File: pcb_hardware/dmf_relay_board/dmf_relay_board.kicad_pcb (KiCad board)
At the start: 2 copper layers, 100 x 100 mm, 34 parts, among them J1 HVPS, J2 Relays to Electrodes 1, J3 Relays to Electrodes 2, J4 Electrodes from Relay 1, J5 Electrodes from Relay 2, U1 HV507

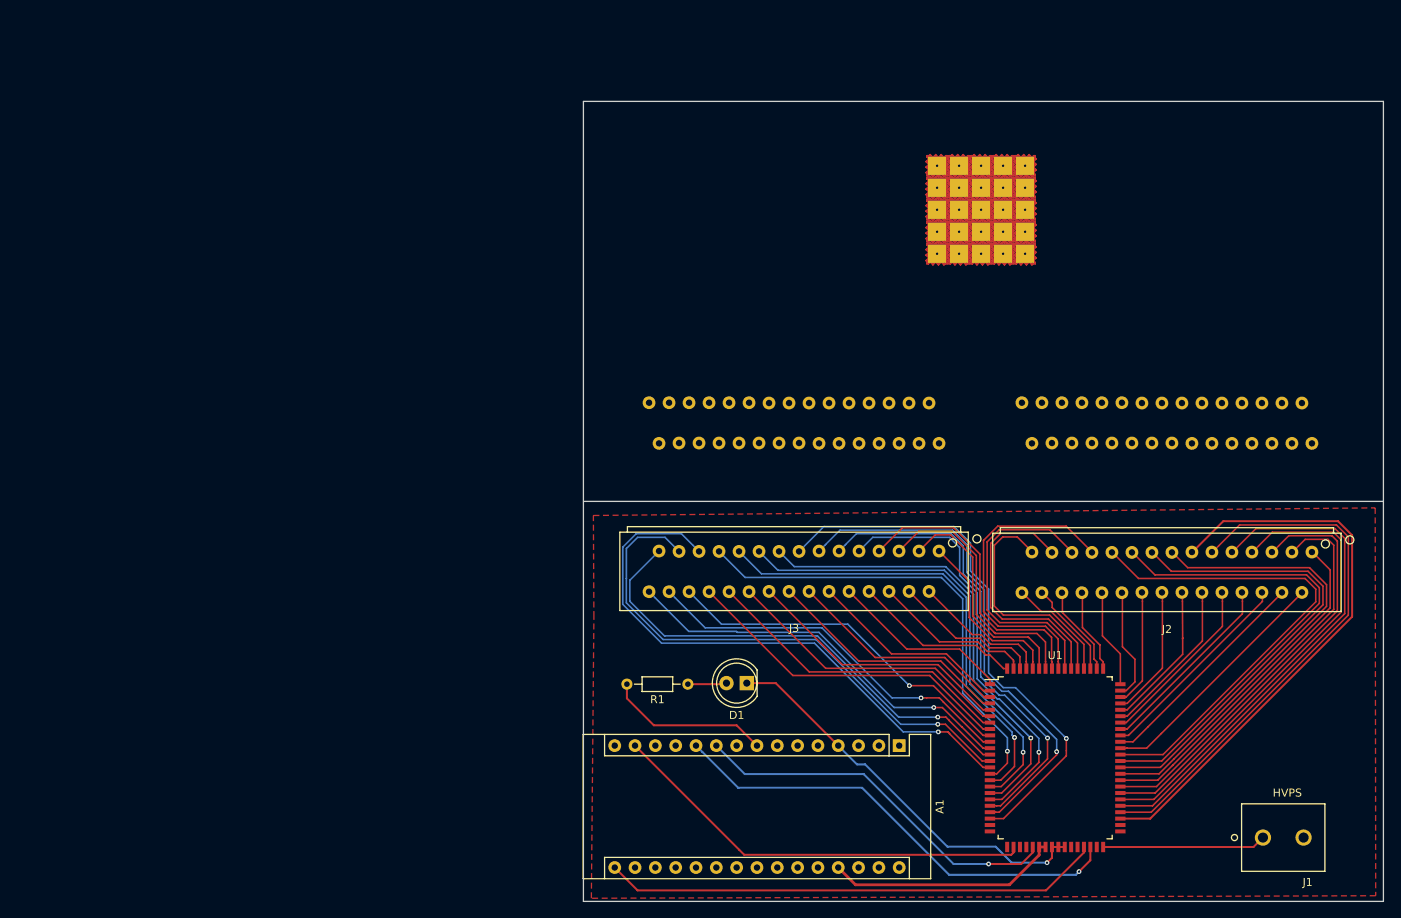
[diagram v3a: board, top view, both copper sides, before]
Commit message: electrode footprints created
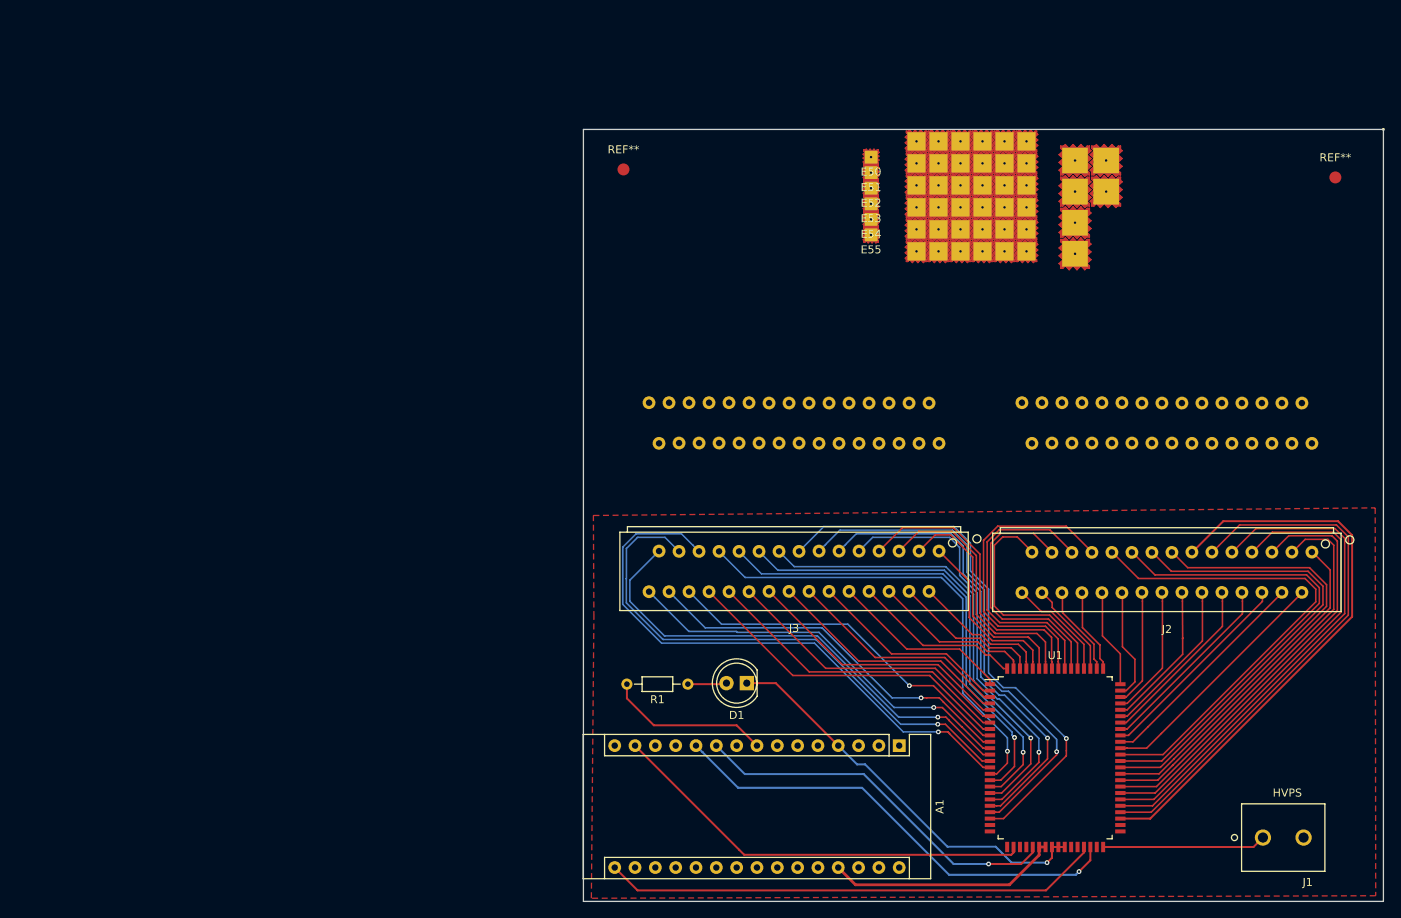
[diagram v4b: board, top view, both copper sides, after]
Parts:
- removed ELEC_1 (x25): FX, GaudiLabsFootPrints:FLUXPAD_2_75_4MIL_4_5
- added E1: ELEC_SML, dmf_relay_board:ELECTRODE_2_75_4MIL_4_5, F.Cu at (153.6, 55.5)
- added E10: ELEC_SML, dmf_relay_board:ELECTRODE_2_75_4MIL_4_5, F.Cu at (161.9, 58.3)
- added E11: ELEC_SML, dmf_relay_board:ELECTRODE_2_75_4MIL_4_5, F.Cu at (164.6, 58.3)
- added E12: ELEC_SML, dmf_relay_board:ELECTRODE_2_75_4MIL_4_5, F.Cu at (167.4, 58.3)
- added E13: ELEC_SML, dmf_relay_board:ELECTRODE_2_75_4MIL_4_5, F.Cu at (153.6, 61.0)
- added E14: ELEC_SML, dmf_relay_board:ELECTRODE_2_75_4MIL_4_5, F.Cu at (156.4, 61.0)
- added E15: ELEC_SML, dmf_relay_board:ELECTRODE_2_75_4MIL_4_5, F.Cu at (159.1, 61.0)
- added E16: ELEC_SML, dmf_relay_board:ELECTRODE_2_75_4MIL_4_5, F.Cu at (161.9, 61.0)
- added E17: ELEC_SML, dmf_relay_board:ELECTRODE_2_75_4MIL_4_5, F.Cu at (164.6, 61.0)
- added E18: ELEC_SML, dmf_relay_board:ELECTRODE_2_75_4MIL_4_5, F.Cu at (167.4, 61.0)
- added E19: ELEC_SML, dmf_relay_board:ELECTRODE_2_75_4MIL_4_5, F.Cu at (153.6, 63.8)
- added E2: ELEC_SML, dmf_relay_board:ELECTRODE_2_75_4MIL_4_5, F.Cu at (156.4, 55.5)
- added E20: ELEC_SML, dmf_relay_board:ELECTRODE_2_75_4MIL_4_5, F.Cu at (156.4, 63.8)
- added E21: ELEC_SML, dmf_relay_board:ELECTRODE_2_75_4MIL_4_5, F.Cu at (159.1, 63.8)
- added E22: ELEC_SML, dmf_relay_board:ELECTRODE_2_75_4MIL_4_5, F.Cu at (161.9, 63.8)
- added E23: ELEC_SML, dmf_relay_board:ELECTRODE_2_75_4MIL_4_5, F.Cu at (164.6, 63.8)
- added E24: ELEC_SML, dmf_relay_board:ELECTRODE_2_75_4MIL_4_5, F.Cu at (167.4, 63.8)
- added E25: ELEC_SML, dmf_relay_board:ELECTRODE_2_75_4MIL_4_5, F.Cu at (153.6, 66.5)
- added E26: ELEC_SML, dmf_relay_board:ELECTRODE_2_75_4MIL_4_5, F.Cu at (156.4, 66.5)
- added E27: ELEC_SML, dmf_relay_board:ELECTRODE_2_75_4MIL_4_5, F.Cu at (159.1, 66.5)
- added E28: ELEC_SML, dmf_relay_board:ELECTRODE_2_75_4MIL_4_5, F.Cu at (161.9, 66.5)
- added E29: ELEC_SML, dmf_relay_board:ELECTRODE_2_75_4MIL_4_5, F.Cu at (164.6, 66.5)
- added E3: ELEC_SML, dmf_relay_board:ELECTRODE_2_75_4MIL_4_5, F.Cu at (159.1, 55.5)
- added E30: ELEC_SML, dmf_relay_board:ELECTRODE_2_75_4MIL_4_5, F.Cu at (167.4, 66.5)
- added E31: ELEC_SML, dmf_relay_board:ELECTRODE_2_75_4MIL_4_5, F.Cu at (153.6, 69.3)
- added E32: ELEC_SML, dmf_relay_board:ELECTRODE_2_75_4MIL_4_5, F.Cu at (156.4, 69.3)
- added E33: ELEC_SML, dmf_relay_board:ELECTRODE_2_75_4MIL_4_5, F.Cu at (159.1, 69.3)
- added E34: ELEC_SML, dmf_relay_board:ELECTRODE_2_75_4MIL_4_5, F.Cu at (161.9, 69.3)
- added E35: ELEC_SML, dmf_relay_board:ELECTRODE_2_75_4MIL_4_5, F.Cu at (164.6, 69.3)
- added E36: ELEC_SML, dmf_relay_board:ELECTRODE_2_75_4MIL_4_5, F.Cu at (167.4, 69.3)
- added E4: ELEC_SML, dmf_relay_board:ELECTRODE_2_75_4MIL_4_5, F.Cu at (161.9, 55.5)
- added E5: ELEC_SML, dmf_relay_board:ELECTRODE_2_75_4MIL_4_5, F.Cu at (164.6, 55.5)
- added E50: ELEC_XS, dmf_relay_board:ELECTRODE_1_375_4MIL_4_5, F.Cu at (147.9, 57.5)
- added E51: ELEC_XS, dmf_relay_board:ELECTRODE_1_375_4MIL_4_5, F.Cu at (147.9, 59.4)
- added E52: ELEC_XS, dmf_relay_board:ELECTRODE_1_375_4MIL_4_5, F.Cu at (147.9, 61.4)
- added E53: ELEC_XS, dmf_relay_board:ELECTRODE_1_375_4MIL_4_5, F.Cu at (147.9, 63.3)
- added E54: ELEC_XS, dmf_relay_board:ELECTRODE_1_375_4MIL_4_5, F.Cu at (147.9, 65.3)
- added E55: ELEC_XS, dmf_relay_board:ELECTRODE_1_375_4MIL_4_5, F.Cu at (147.9, 67.2)
- added E6: ELEC_SML, dmf_relay_board:ELECTRODE_2_75_4MIL_4_5, F.Cu at (167.4, 55.5)
- added E60: ELEC_LG, dmf_relay_board:ELECTRODE_3_89_4MIL_4_5, F.Cu at (173.4, 57.9)
- added E61: ELEC_LG, dmf_relay_board:ELECTRODE_3_89_4MIL_4_5, F.Cu at (173.4, 61.8)
- added E62: ELEC_LG, dmf_relay_board:ELECTRODE_3_89_4MIL_4_5, F.Cu at (173.4, 65.7)
- added E63: ELEC_LG, dmf_relay_board:ELECTRODE_3_89_4MIL_4_5, F.Cu at (173.4, 69.6)
- added E64: ELEC_LG, dmf_relay_board:ELECTRODE_3_89_4MIL_4_5, F.Cu at (177.3, 57.9)
- added E65: ELEC_LG, dmf_relay_board:ELECTRODE_3_89_4MIL_4_5, F.Cu at (177.3, 61.8)
- added E7: ELEC_SML, dmf_relay_board:ELECTRODE_2_75_4MIL_4_5, F.Cu at (153.6, 58.3)
- added E8: ELEC_SML, dmf_relay_board:ELECTRODE_2_75_4MIL_4_5, F.Cu at (156.4, 58.3)
- added E9: ELEC_SML, dmf_relay_board:ELECTRODE_2_75_4MIL_4_5, F.Cu at (159.1, 58.3)
- added REF**: Fiducial_1.5mm_Mask3mm, Fiducial:Fiducial_1.5mm_Mask3mm, F.Cu at (206.0, 60.0)
- added REF**: Fiducial_1.5mm_Mask3mm, Fiducial:Fiducial_1.5mm_Mask3mm, F.Cu at (117.0, 59.0)
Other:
- board size 100 x 100 mm -> 100 x 96.5 mm

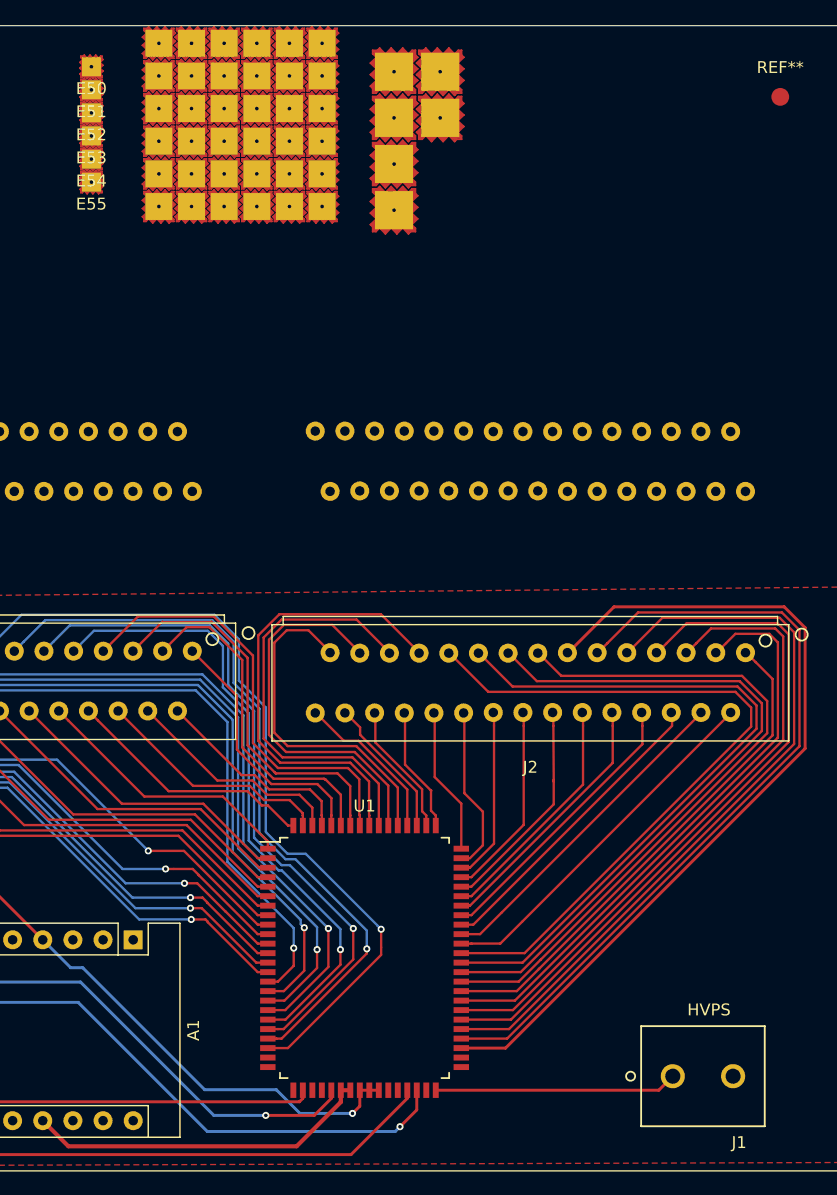
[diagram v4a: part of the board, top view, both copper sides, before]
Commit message: XS to SM electrodes cmplt
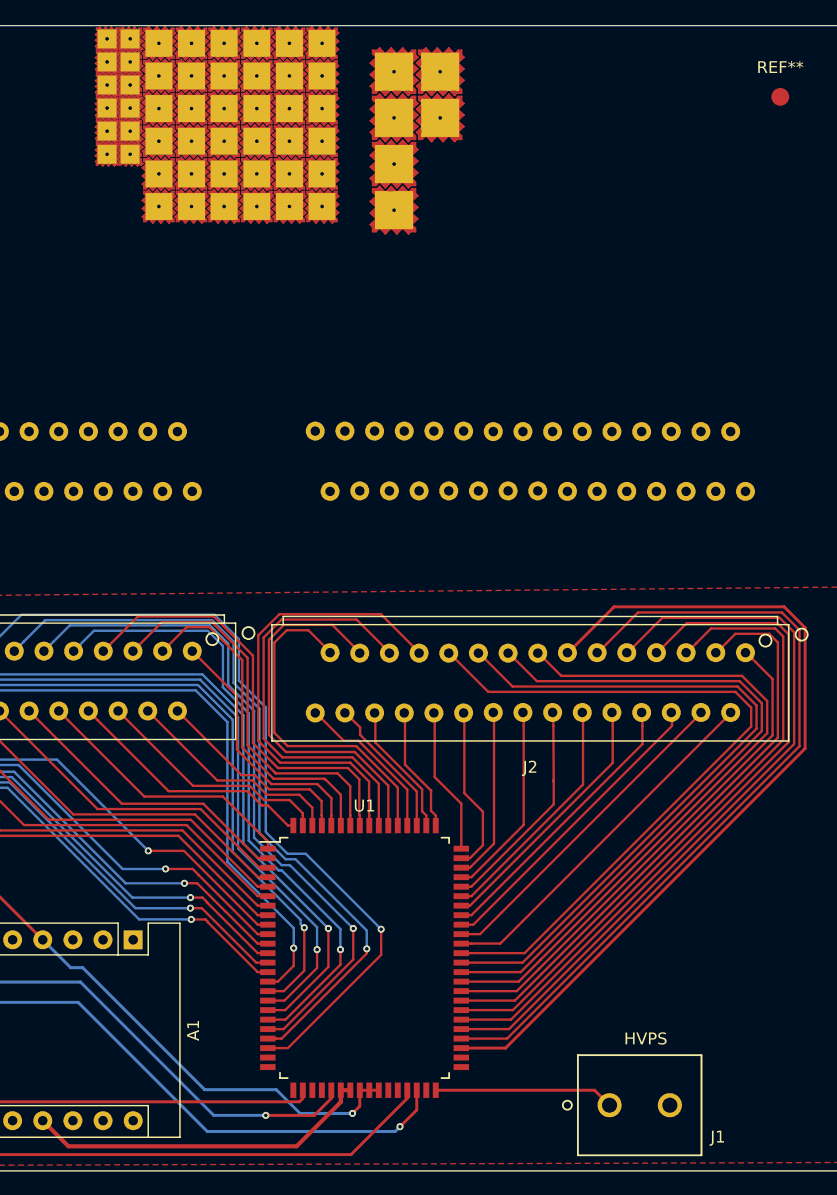
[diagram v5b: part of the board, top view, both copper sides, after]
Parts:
- added REF**: E_XS_SM_6, dmf_relay_board:ELEC_XS_TO_SM_NUM6, F.Cu at (151.2, 64.9)
- added REF**: E_XS_SM_5, dmf_relay_board:ELEC_XS_TO_SM_NUM5, F.Cu at (151.2, 62.9)
- added REF**: E_XS_SM_4, dmf_relay_board:ELEC_XS_TO_SM_NUM4, F.Cu at (151.2, 61.0)
- added REF**: ELEC_XS_TO_SM_NUM3, dmf_relay_board:ELEC_XS_TO_SM_NUM3, F.Cu at (151.2, 59.0)
- added REF**: E_XS_SM_2, dmf_relay_board:ELEC_XS_TO_SM_NUM2, F.Cu at (151.2, 57.1)
- added REF**: E_XS_SM_1, dmf_relay_board:ELEC_XS_TO_SM_NUM1, F.Cu at (151.2, 55.2)
- moved J1 5.86 mm to (191.6, 145.0)
- moved E50 2.69 mm to (149.2, 55.2)
- moved E51 2.69 mm to (149.2, 57.1)
- moved E52 2.69 mm to (149.2, 59.0)
- moved E53 2.69 mm to (149.2, 61.0)
- moved E55 2.69 mm to (149.2, 64.9)
- moved E54 2.69 mm to (149.2, 62.9)
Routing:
- net VPP: track 20.5 -> 15.2 mm

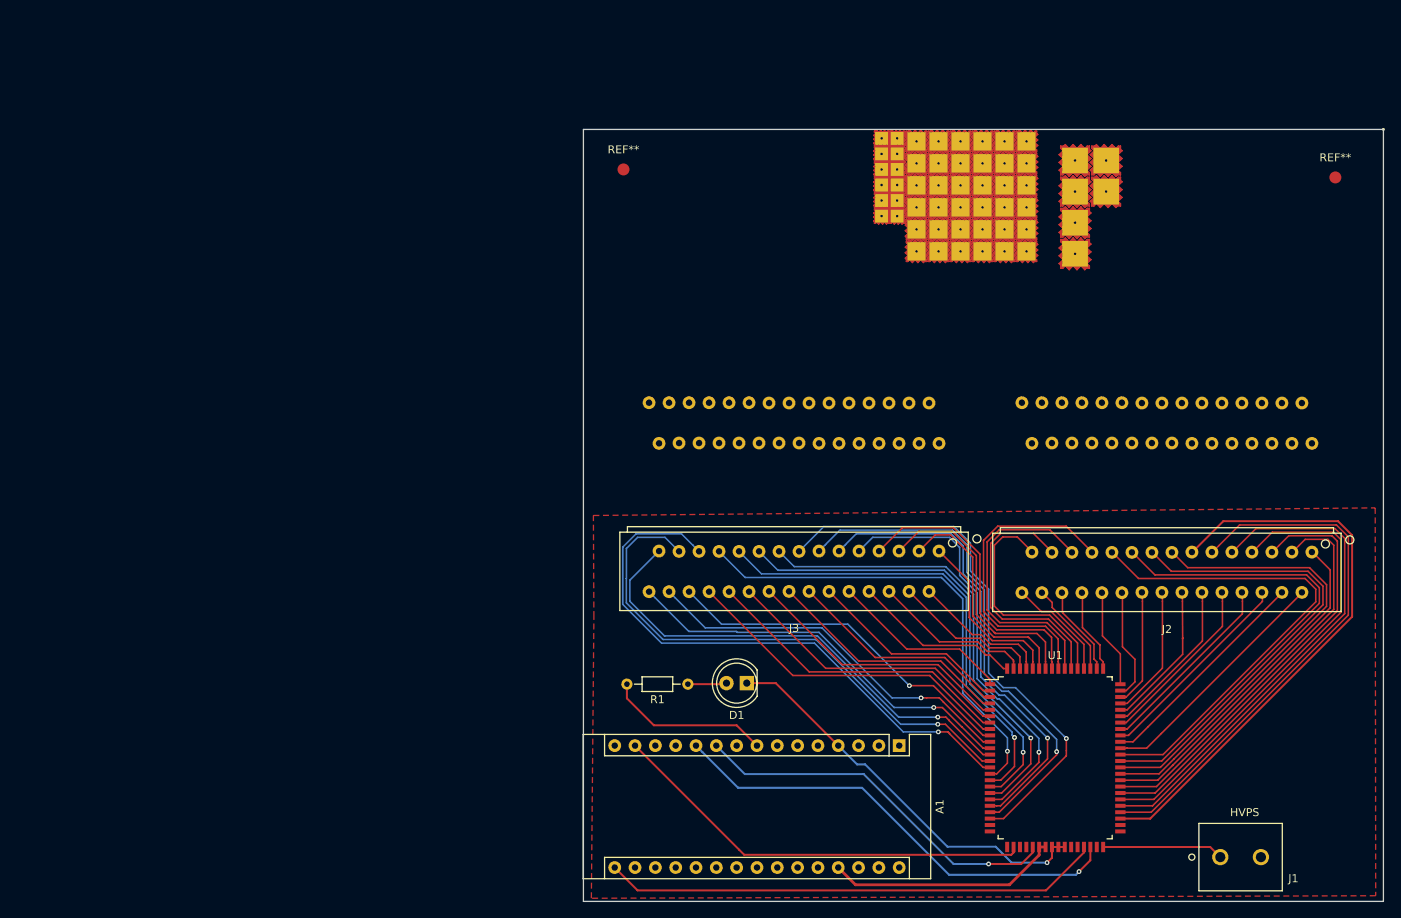
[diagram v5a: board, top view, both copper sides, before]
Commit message: electrodes completed
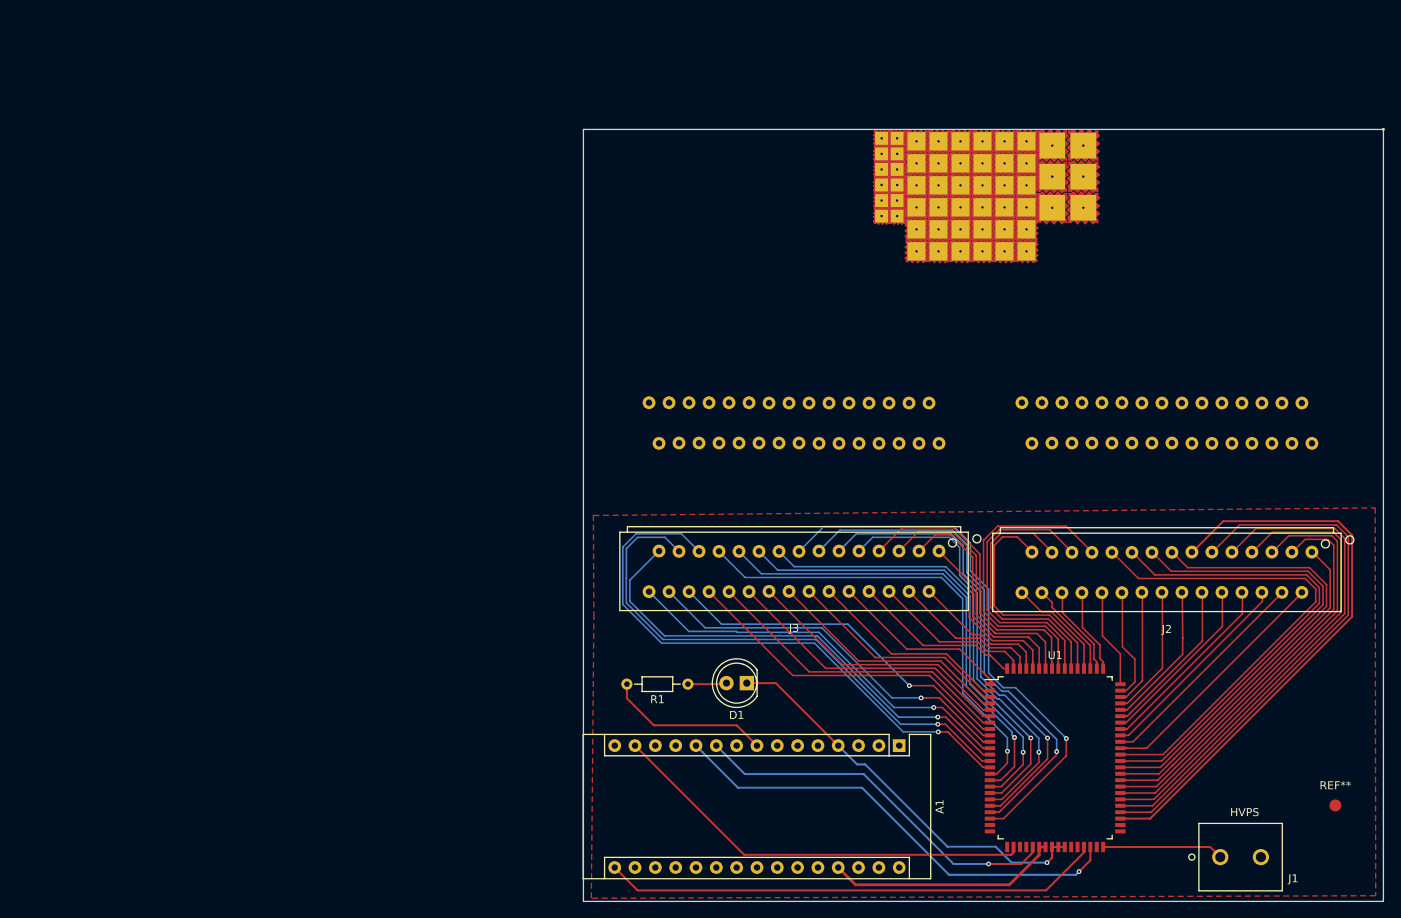
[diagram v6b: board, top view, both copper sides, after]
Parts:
- removed E60, E61, E62, E63, E64, E65: ELEC_LG, dmf_relay_board:ELECTRODE_3_89_4MIL_4_5
- removed the REF** at (206.0, 60.0)
- removed the REF** at (117.0, 59.0)
- added REF**: E_LG, dmf_relay_board:ELECTRODE_3_89_4MIL_4_5, F.Cu at (174.5, 63.8)
- added REF**: E_LG, dmf_relay_board:ELECTRODE_3_89_4MIL_4_5, F.Cu at (174.5, 59.9)
- added REF**: E_LG, dmf_relay_board:ELECTRODE_3_89_4MIL_4_5, F.Cu at (174.5, 56.1)
- added REF**: Fiducial_1.5mm_Mask3mm, Fiducial:Fiducial_1.5mm_Mask3mm, F.Cu at (206.0, 138.5)
- added REF**: E_SM_LG_3, dmf_relay_board:ELEC_SM_TO_LG_NUM3, F.Cu at (170.6, 63.8)
- added REF**: E_SM_LG_2, dmf_relay_board:ELEC_SM_TO_LG_NUM2, F.Cu at (170.6, 59.9)
- added REF**: E_SM_LG_1, dmf_relay_board:ELEC_SM_TO_LG_NUM1, F.Cu at (170.6, 56.1)
